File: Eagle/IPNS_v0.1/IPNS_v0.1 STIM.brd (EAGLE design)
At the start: 100 x 80 mm, 9 parts, among them U1 LTC3459ES6TRMPBF, U2 LT1492CS8TRPBF

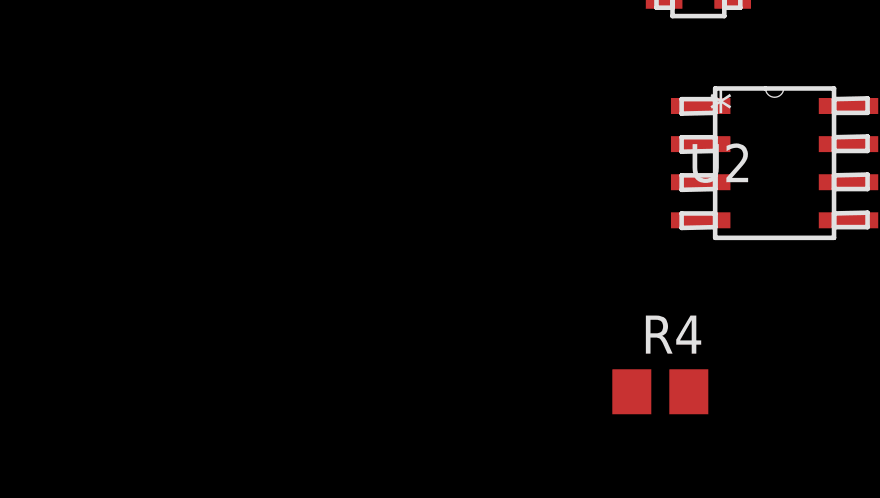
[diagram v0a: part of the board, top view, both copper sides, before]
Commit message: Developed a CAD model for the mosfet part
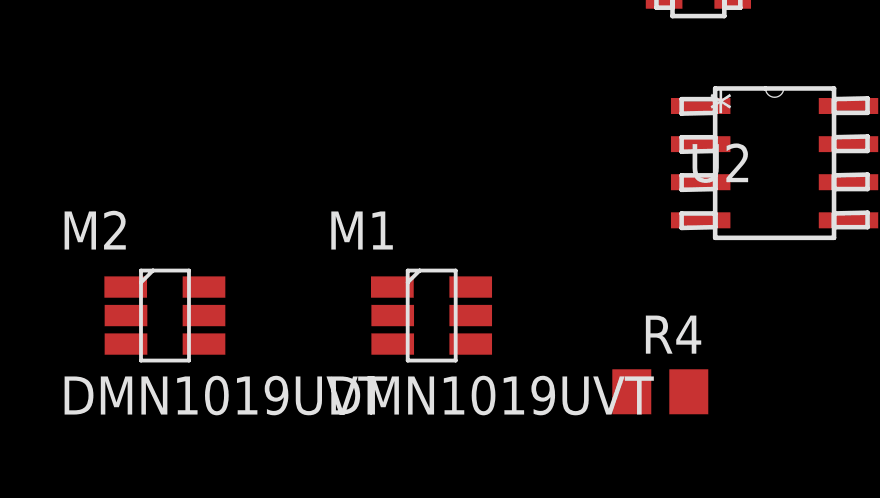
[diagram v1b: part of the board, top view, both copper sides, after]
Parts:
- added M1, M2: DMN1019UVT, IPNS_Lib_v0.1:DMN1019UVT
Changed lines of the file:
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@@
 </element>
 <element name="R4" library="IPNS_Lib_v0.1" package="R0805" value="" x="-27.94" y="-3.81"/>
+<element name="M1" library="IPNS_Lib_v0.1" package="DMN1019UVT" value="DMN1019UVT" x="-35.56" y="-1.27"/>
+<element name="M2" library="IPNS_Lib_v0.1" package="DMN1019UVT" value="DMN1019UVT" x="-44.45" y="-1.27"/>
 </elements>
 <signals>
